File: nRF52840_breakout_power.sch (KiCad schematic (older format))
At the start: 14 parts, among them Q1 pmos, U2 AP2112K-3.3, U3 MCP73831-2-OT

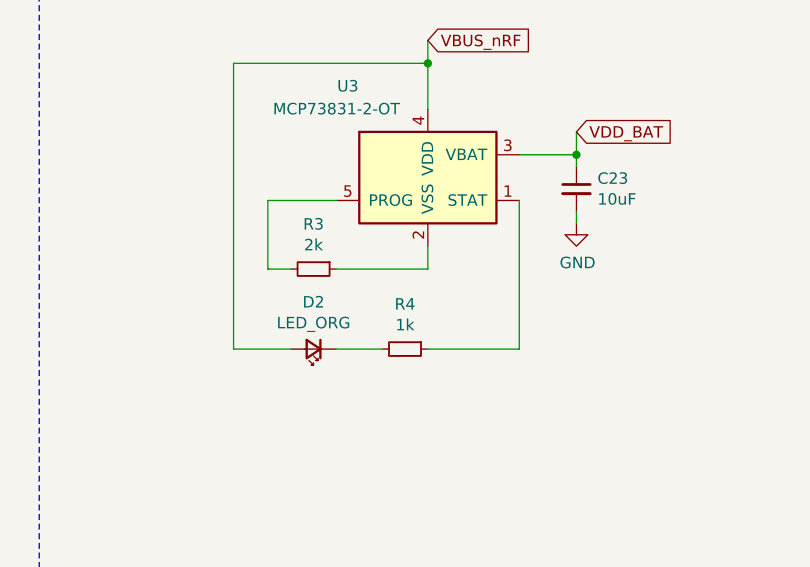
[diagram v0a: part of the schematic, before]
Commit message: add missing gnd to charge ic
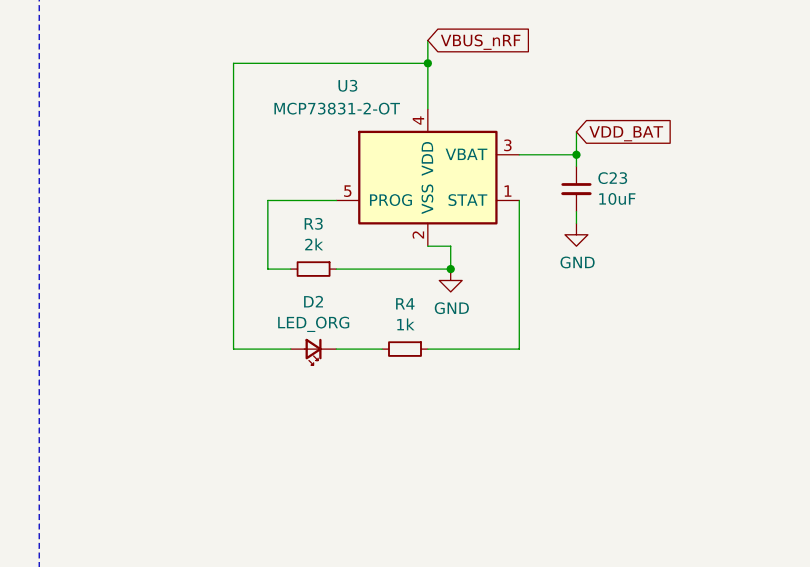
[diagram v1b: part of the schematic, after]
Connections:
- net GND: now also R3.1, U3.2 (VSS)
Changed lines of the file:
@@
-	1    0    0    -1
-$EndComp
-$Comp
-L Battery_Management:MCP73831-2-OT U3
-U 1 1 5D376B89
-P 8000 1800
-F 0 "U3" H 7650 2200 50  0000 C CNN
-F 1 "MCP73831-2-OT" H 7600 2100 50  0000 C CNN
-F 2 "Package_TO_SOT_SMD:SOT-23-5" H 8050 1550 50  0001 L CIN
-F 3 "http://ww1.microchip.com/downloads/en/DeviceDoc/20001984g.pdf" H 7850 1750 50  0001 C CNN
-F 4 " MCP73831T-2ATI/OTCT-ND " H 8000 1800 50  0001 C CNN "Digikey"
-F 5 "MCP73831T-2ATI/OT" H 8000 1800 50  0001 C CNN "MFG P/N"
-F 6 " IC CONTROLLR LI-ION 4.2V SOT23-5 " H 8000 1800 50  0001 C CNN "Description"
-F 7 "C14879" H 8000 1800 50  0001 C CNN "LCSC"
-F 8 "Microchip Tech" H 8000 1800 50  0001 C CNN "Manufacturer"
-	1    8000 1800
 	1    0    0    -1
 $EndComp
@@
 	8400 1900 8400 2550
 Wire Wire Line
-	7600 2200 8000 2200
-Wire Wire Line
-	8000 2200 8000 2100
+	7600 2200 8100 2200
 Wire Wire Line
 	7400 2200 7300 2200
@@
 	0    -1   -1   0
 $EndComp
+$Comp
+L power:GND #PWR?
+U 1 1 5F900D9B
+P 8100 2200
+F 0 "#PWR?" H 8100 1950 50  0001 C CNN
+F 1 "GND" H 8105 2027 50  0000 C CNN
+F 2 "" H 8100 2200 50  0001 C CNN
+F 3 "" H 8100 2200 50  0001 C CNN
+	1    8100 2200
+	1    0    0    -1
+$EndComp
+$Comp
+L Battery_Management:MCP73831-2-OT U3
+U 1 1 5D376B89
+P 8000 1800
+F 0 "U3" H 7650 2200 50  0000 C CNN
+F 1 "MCP73831-2-OT" H 7600 2100 50  0000 C CNN
+F 2 "Package_TO_SOT_SMD:SOT-23-5" H 8050 1550 50  0001 L CIN
+F 3 "http://ww1.microchip.com/downloads/en/DeviceDoc/20001984g.pdf" H 7850 1750 50  0001 C CNN
+F 4 " MCP73831T-2ATI/OTCT-ND " H 8000 1800 50  0001 C CNN "Digikey"
+F 5 "MCP73831T-2ATI/OT" H 8000 1800 50  0001 C CNN "MFG P/N"
+F 6 " IC CONTROLLR LI-ION 4.2V SOT23-5 " H 8000 1800 50  0001 C CNN "Description"
+F 7 "C14879" H 8000 1800 50  0001 C CNN "LCSC"
+F 8 "Microchip Tech" H 8000 1800 50  0001 C CNN "Manufacturer"
+	1    8000 1800
+	1    0    0    -1
+$EndComp
+Wire Wire Line
+	8000 2100 8100 2100
+Wire Wire Line
+	8100 2100 8100 2200
+Connection ~ 8100 2200
 $EndSCHEMATC
